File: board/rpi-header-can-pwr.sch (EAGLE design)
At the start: 40 parts, among them U1 MCP2515, X1 RJ45-8L21-S, X2 RJ45-8L21-S

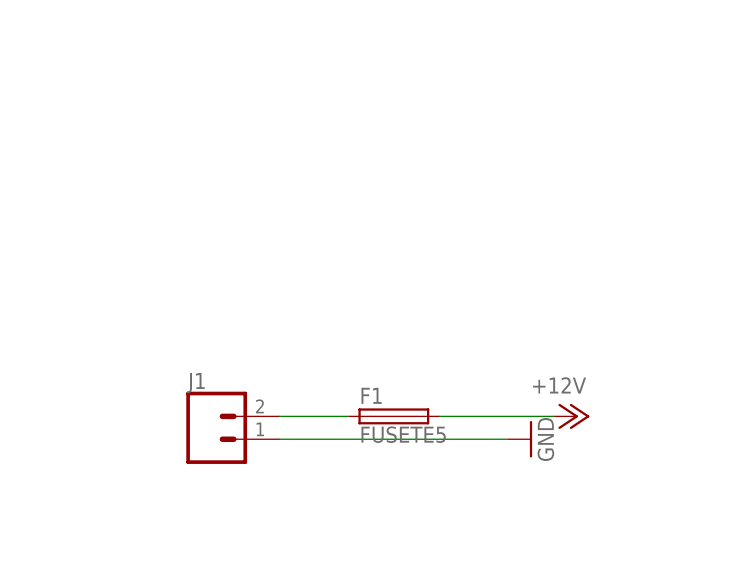
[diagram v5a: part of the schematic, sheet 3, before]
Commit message: add varistor
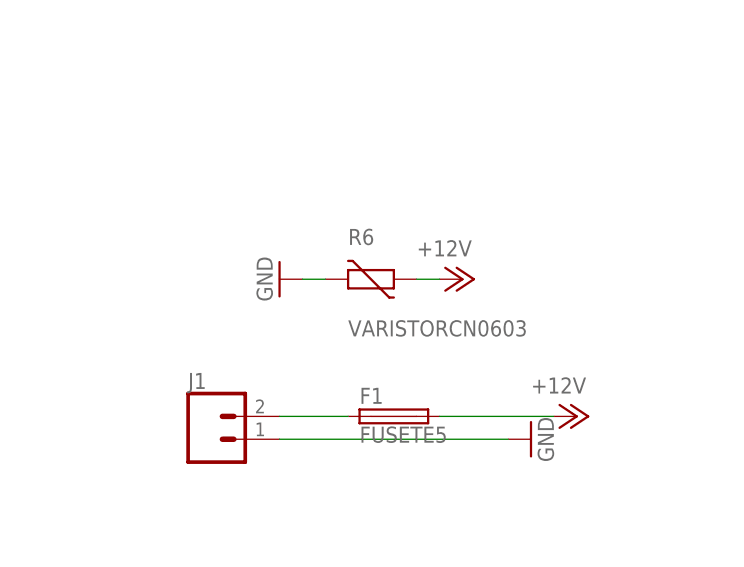
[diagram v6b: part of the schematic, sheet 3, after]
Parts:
- added R6: VARISTORCN0603, varistor:VARISTORCN0603
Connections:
- net +12V: now also R6.1
- net GND: now also R6.2
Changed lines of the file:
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@@
 <grid distance="0.1" unitdist="inch" unit="inch" style="lines" multiple="1" display="no" altdistance="0.01" altunitdist="inch" altunit="inch"/>
 <layers>
-<layer number="1" name="Top" color="4" fill="1" visible="yes" active="no"/>
-<layer number="2" name="Route2" color="1" fill="3" visible="yes" active="no"/>
-<layer number="3" name="Route3" color="4" fill="3" visible="yes" active="no"/>
-<layer number="4" name="Route4" color="1" fill="4" visible="yes" active="no"/>
-<layer number="5" name="Route5" color="4" fill="4" visible="yes" active="no"/>
-<layer number="6" name="Route6" color="1" fill="8" visible="yes" active="no"/>
-<layer number="7" name="Route7" color="4" fill="8" visible="yes" active="no"/>
-<layer number="8" name="Route8" color="1" fill="2" visible="yes" active="no"/>
-<layer number="9" name="Route9" color="4" fill="2" visible="yes" active="no"/>
-<layer number="10" name="Route10" color="1" fill="7" visible="yes" active="no"/>
-<layer number="11" name="Route11" color="4" fill="7" visible="yes" active="no"/>
-<layer number="12" name="Route12" color="1" fill="5" visible="yes" active="no"/>
-<layer number="13" name="Route13" color="4" fill="5" visible="yes" active="no"/>
-<layer number="14" name="Route14" color="1" fill="6" visible="yes" active="no"/>
-<layer number="15" name="Route15" color="4" fill="6" visible="yes" active="no"/>
-<layer number="16" name="Bottom" color="1" fill="1" visible="yes" active="no"/>
-<layer number="17" name="Pads" color="2" fill="1" visible="yes" active="no"/>
-<layer number="18" name="Vias" color="2" fill="1" visible="yes" active="no"/>
-<layer number="19" name="Unrouted" color="6" fill="1" visible="yes" active="no"/>
-<layer number="20" name="Dimension" color="15" fill="1" visible="yes" active="no"/>
-<layer number="21" name="tPlace" color="7" fill="1" visible="yes" active="no"/>
-<layer number="22" name="bPlace" color="7" fill="1" visible="yes" active="no"/>
-<layer number="23" name="tOrigins" color="15" fill="1" visible="yes" active="no"/>
-<layer number="24" name="bOrigins" color="15" fill="1" visible="yes" active="no"/>
-<layer number="25" name="tNames" color="7" fill="1" visible="yes" active="no"/>
-<layer number="26" name="bNames" color="7" fill="1" visible="yes" active="no"/>
-<layer number="27" name="tValues" color="7" fill="1" visible="yes" active="no"/>
-<layer number="28" name="bValues" color="7" fill="1" visible="yes" active="no"/>
+<layer number="1" name="Top" color="4" fill="1" visible="no" active="no"/>
+<layer number="2" name="Route2" color="1" fill="3" visible="no" active="no"/>
+<layer number="3" name="Route3" color="4" fill="3" visible="no" active="no"/>
+<layer number="4" name="Route4" color="1" fill="4" visible="no" active="no"/>
+<layer number="5" name="Route5" color="4" fill="4" visible="no" active="no"/>
+<layer number="6" name="Route6" color="1" fill="8" visible="no" active="no"/>
+<layer number="7" name="Route7" color="4" fill="8" visible="no" active="no"/>
+<layer number="8" name="Route8" color="1" fill="2" visible="no" active="no"/>
+<layer number="9" name="Route9" color="4" fill="2" visible="no" active="no"/>
+<layer number="10" name="Route10" color="1" fill="7" visible="no" active="no"/>
+<layer number="11" name="Route11" color="4" fill="7" visible="no" active="no"/>
+<layer number="12" name="Route12" color="1" fill="5" visible="no" active="no"/>
+<layer number="13" name="Route13" color="4" fill="5" visible="no" active="no"/>
+<layer number="14" name="Route14" color="1" fill="6" visible="no" active="no"/>
+<layer number="15" name="Route15" color="4" fill="6" visible="no" active="no"/>
+<layer number="16" name="Bottom" color="1" fill="1" visible="no" active="no"/>
+<layer number="17" name="Pads" color="2" fill="1" visible="no" active="no"/>
+<layer number="18" name="Vias" color="2" fill="1" visible="no" active="no"/>
+<layer number="19" name="Unrouted" color="6" fill="1" visible="no" active="no"/>
+<layer number="20" name="Dimension" color="15" fill="1" visible="no" active="no"/>
+<layer number="21" name="tPlace" color="7" fill="1" visible="no" active="no"/>
+<layer number="22" name="bPlace" color="7" fill="1" visible="no" active="no"/>
+<layer number="23" name="tOrigins" color="15" fill="1" visible="no" active="no"/>
+<layer number="24" name="bOrigins" color="15" fill="1" visible="no" active="no"/>
+<layer number="25" name="tNames" color="7" fill="1" visible="no" active="no"/>
+<layer number="26" name="bNames" color="7" fill="1" visible="no" active="no"/>
+<layer number="27" name="tValues" color="7" fill="1" visible="no" active="no"/>
+<layer number="28" name="bValues" color="7" fill="1" visible="no" active="no"/>
 <layer number="29" name="tStop" color="7" fill="3" visible="no" active="no"/>
 <layer number="30" name="bStop" color="7" fill="6" visible="no" active="no"/>
@@
 <layer number="35" name="tGlue" color="7" fill="4" visible="no" active="no"/>
 <layer number="36" name="bGlue" color="7" fill="5" visible="no" active="no"/>
-<layer number="37" name="tTest" color="7" fill="1" visible="yes" active="no"/>
-<layer number="38" name="bTest" color="7" fill="1" visible="yes" active="no"/>
+<layer number="37" name="tTest" color="7" fill="1" visible="no" active="no"/>
+<layer number="38" name="bTest" color="7" fill="1" visible="no" active="no"/>
 <layer number="39" name="tKeepout" color="4" fill="11" visible="no" active="no"/>
 <layer number="40" name="bKeepout" color="1" fill="11" visible="no" active="no"/>
@@
 <layer number="44" name="Drills" color="7" fill="1" visible="no" active="no"/>
 <layer number="45" name="Holes" color="7" fill="1" visible="no" active="no"/>
-<layer number="46" name="Milling" color="3" fill="1" visible="yes" active="no"/>
-<layer number="47" name="Measures" color="7" fill="1" visible="yes" active="no"/>
-<layer number="48" name="Document" color="7" fill="1" visible="yes" active="no"/>
-<layer number="49" name="Reference" color="7" fill="1" visible="yes" active="no"/>
-<layer number="50" name="dxf" color="7" fill="1" visible="yes" active="no"/>
-<layer number="51" name="tDocu" color="7" fill="1" visible="yes" active="no"/>
-<layer number="52" name="bDocu" color="7" fill="1" visible="yes" active="no"/>
-<layer number="53" name="tGND_GNDA" color="7" fill="1" visible="yes" active="no"/>
-<layer number="54" name="bGND_GNDA" color="7" fill="1" visible="yes" active="no"/>
-<layer number="56" name="wert" color="7" fill="1" visible="yes" active="no"/>
-<layer number="57" name="tCAD" color="7" fill="1" visible="yes" active="no"/>
-<layer number="59" name="tCarbon" color="7" fill="1" visible="yes" active="no"/>
-<layer number="60" name="bCarbon" color="7" fill="1" visible="yes" active="no"/>
+<layer number="46" name="Milling" color="3" fill="1" visible="no" active="no"/>
+<layer number="47" name="Measures" color="7" fill="1" visible="no" active="no"/>
+<layer number="48" name="Document" color="7" fill="1" visible="no" active="no"/>
+<layer number="49" name="Reference" color="7" fill="1" visible="no" active="no"/>
+<layer number="50" name="dxf" color="7" fill="1" visible="no" active="no"/>
+<layer number="51" name="tDocu" color="7" fill="1" visible="no" active="no"/>
+<layer number="52" name="bDocu" color="7" fill="1" visible="no" active="no"/>
+<layer number="53" name="tGND_GNDA" color="7" fill="1" visible="no" active="no"/>
+<layer number="54" name="bGND_GNDA" color="7" fill="1" visible="no" active="no"/>
+<layer number="56" name="wert" color="7" fill="1" visible="no" active="no"/>
+<layer number="57" name="tCAD" color="7" fill="1" visible="no" active="no"/>
+<layer number="59" name="tCarbon" color="7" fill="1" visible="no" active="no"/>
+<layer number="60" name="bCarbon" color="7" fill="1" visible="no" active="no"/>
 <layer number="90" name="Modules" color="5" fill="1" visible="yes" active="yes"/>
 <layer number="91" name="Nets" color="2" fill="1" visible="yes" active="yes"/>
@@
 <part name="F2" library="fuse" deviceset="FUSE" device="LITTLEFUSE"/>
 <part name="F3" library="fuse" deviceset="FUSE" device="TE5"/>
+<part name="R6" library="varistor" deviceset="VARISTOR" device="CN0603"/>
+<part name="P+5" library="supply1" deviceset="+12V" device=""/>
+<part name="GND20" library="supply1" deviceset="GND" device=""/>
 </parts>
 <sheets>
@@
 <instance part="F1" gate="G$1" x="172.72" y="78.74"/>
 <instance part="F2" gate="G$1" x="187.96" y="43.18"/>
+<instance part="R6" gate="G$1" x="170.18" y="93.98"/>
+<instance part="P+5" gate="1" x="180.34" y="93.98" rot="R270"/>
+<instance part="GND20" gate="1" x="160.02" y="93.98" rot="R270"/>
 </instances>
 <busses>
@@
 <pinref part="F1" gate="G$1" pin="2"/>
 </segment>
+<segment>
+<pinref part="R6" gate="G$1" pin="1"/>
+<pinref part="P+5" gate="1" pin="+12V"/>
+<wire x1="175.26" y1="93.98" x2="177.8" y2="93.98" width="0.1524" layer="91"/>
+</segment>
 </net>
 <net name="GND" class="0">
@@
 <pinref part="J1" gate="G$1" pin="1"/>
 </segment>
-</net>
+<segment>
+<pinref part="R6" gate="G$1" pin="2"/>
+<pinref part="GND20" gate="1" pin="GND"/>
+<wire x1="162.56" y1="93.98" x2="165.1" y2="93.98" width="0.1524" layer="91"/>
+</segment>
+</net>

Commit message: add holes for rpi zero
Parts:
- RPI1: value RASPBERRYPI_BPLUS_HATSLOTS -> RASPBERRYPI_BPLUS_HATNOSLOTS; device microbuilder:RASPBERRYPI_BPLUS_HATSLOTS -> microbuilder:RASPBERRYPI_BPLUS_HATNOSLOTS
